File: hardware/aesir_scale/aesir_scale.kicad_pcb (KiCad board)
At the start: 2 copper layers, 60 x 50 mm, 48 parts, among them J1 jst xh 4, J2 jst gh, J3 jst xh 4, J4 jst_sh 6, J5 jst gh, J6 USB_C_Receptacle_USB2.0, U1 STM32U575CGTx, U2 NAU7802SGI, U3 AZ1117CH2-3.3TRG1, U4 TJA1051T, Y1 48MHz

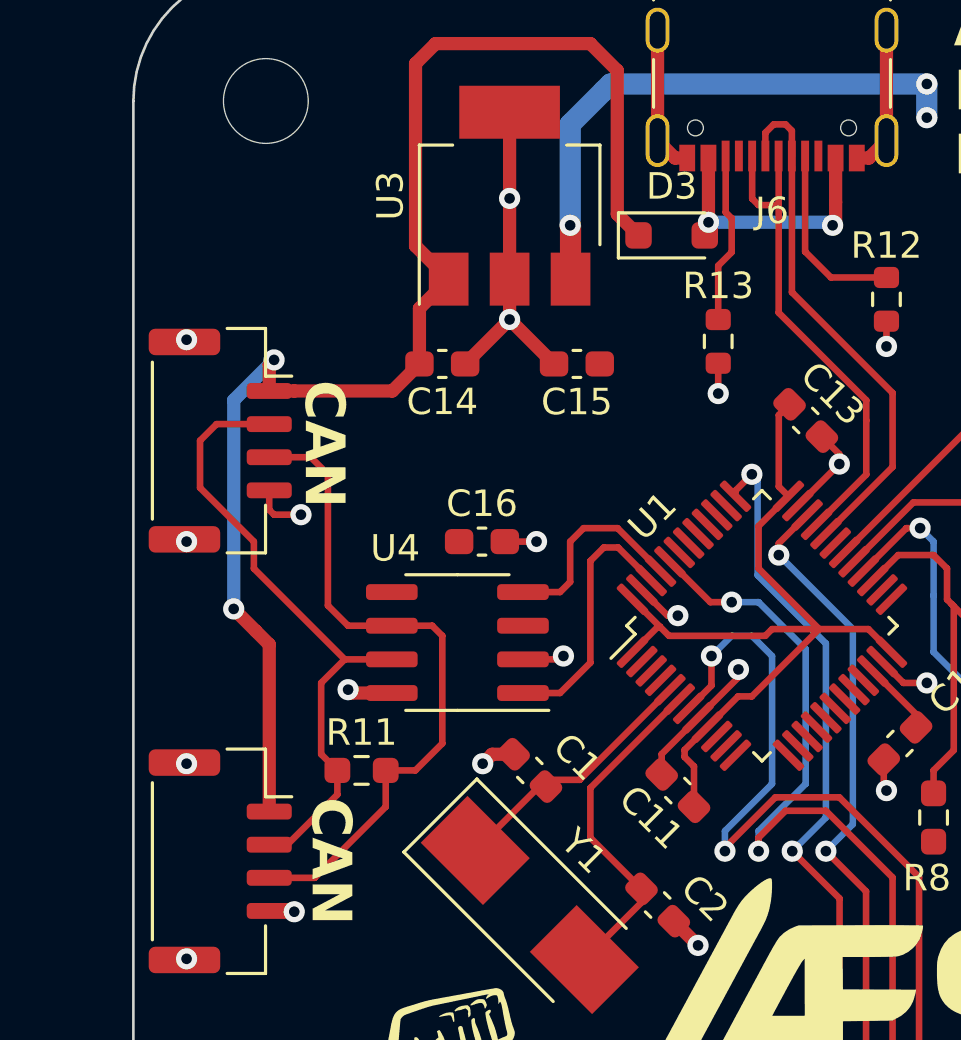
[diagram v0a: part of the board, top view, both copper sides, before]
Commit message: USB diode & CAN jumper
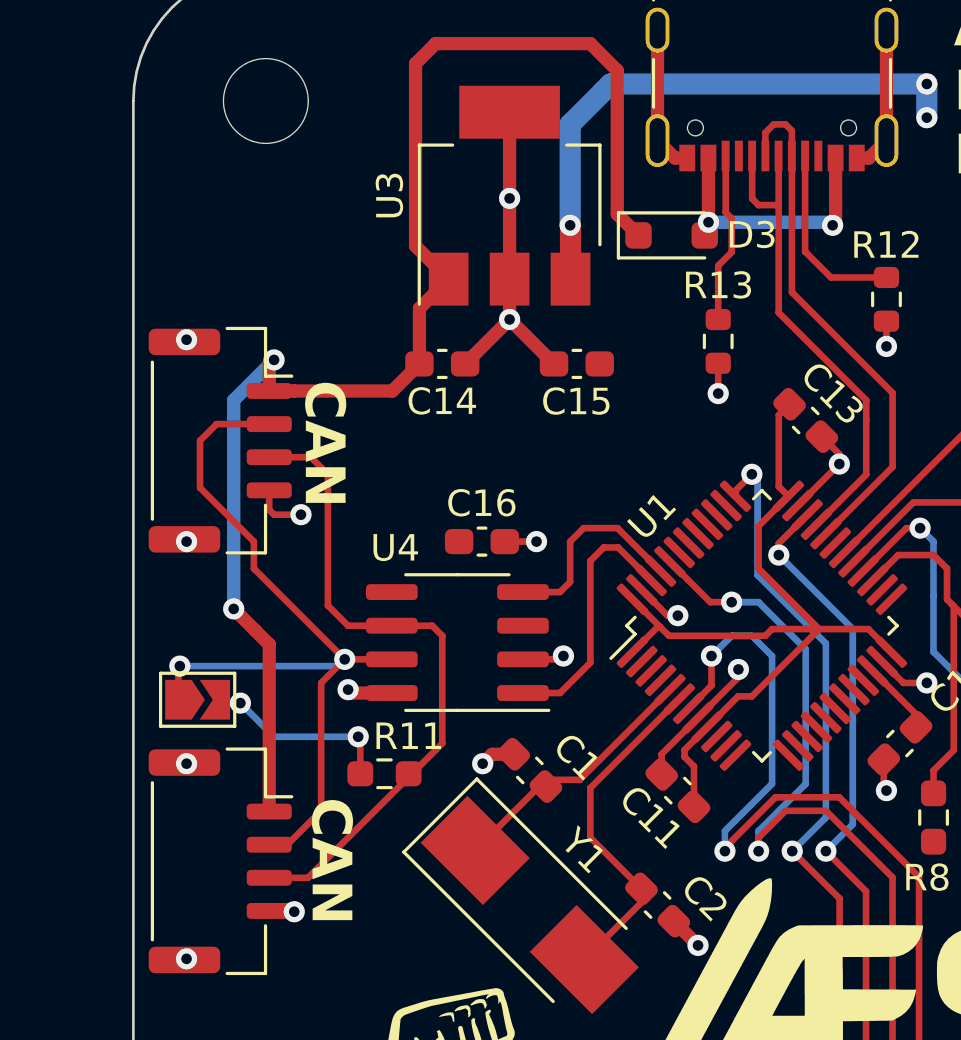
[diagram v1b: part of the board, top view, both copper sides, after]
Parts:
- added JP1: SolderJumper_2_Open, Jumper:SolderJumper-2_P1.3mm_Open_TrianglePad1.0x1.5mm, F.Cu at (64.4, 93.6)
- moved R11 0.87 mm to (71.5, 96.4)
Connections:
- R11 pad 1: /CAN_H -> Net-(JP1-B)
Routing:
- net Net-(JP1-B): track 0.00 -> 7.34 mm, vias 0 -> 2
- net /CAN_H: track 24.2 -> 31.4 mm, vias 0 -> 2
- net /CAN_L: track 26.2 -> 24.9 mm
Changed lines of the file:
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@@
   (net 62 "VCC")
   (net 63 "Net-(D3-A)")
+  (net 64 "Net-(JP1-B)")
   (footprint "Package_SO:SOIC-8_3.9x4.9mm_P1.27mm" (layer "F.Cu")
     (at 74.23 91.44 180)
@@
     (property "mfn" " USB4105-GF-A ")
     (attr smd)
-    (fp_text reference "J6" (at 0 -4.58) (layer "F.SilkS")
+    (fp_text reference "J6" (at 0 -4.58) (layer "F.SilkS") hide
         (effects (font (size 1 1) (thickness 0.15)))
     )
@@
   )
   (footprint "Resistor_SMD:R_0603_1608Metric_Pad0.98x0.95mm_HandSolder" (layer "F.Cu")
-    (at 70.612 96.266)
+    (at 71.4775 96.393)
     (descr "Resistor SMD 0603 (1608 Metric), square (rectangular) end terminal, IPC_7351 nominal with elongated pad for handsoldering. (Body size source: IPC-SM-782 page 72, https://www.pcb-3d.com/wordpress/wp-content/uploads/ipc-sm-782a_amendment_1_and_2.pdf), generated with kicad-footprint-generator")
     (tags "resistor handsolder")
@@
     (property "ki_keywords" "R resistor")
     (attr smd)
-    (fp_text reference "R11" (at 0 -1.43) (layer "F.SilkS")
+    (fp_text reference "R11" (at 0.9125 -1.397) (layer "F.SilkS")
         (effects (font (size 1 1) (thickness 0.15)))
     )
@@
       (stroke (width 0.1) (type solid)) (layer "F.Fab"))
     (pad "1" smd roundrect (at -0.9125 0) (size 0.975 0.95) (layers "F.Cu" "F.Paste" "F.Mask") (roundrect_rratio 0.25)
-      (net 32 "/CAN_H") (pintype "passive"))
+      (net 64 "Net-(JP1-B)") (pintype "passive"))
     (pad "2" smd roundrect (at 0.9125 0) (size 0.975 0.95) (layers "F.Cu" "F.Paste" "F.Mask") (roundrect_rratio 0.25)
       (net 33 "/CAN_L") (pintype "passive"))
@@
     (property "ki_keywords" "diode")
     (attr smd)
-    (fp_text reference "D3" (at 0 -1.85) (layer "F.SilkS")
+    (fp_text reference "D3" (at 3.028 0) (layer "F.SilkS")
         (effects (font (size 1 1) (thickness 0.15)))
     )
@@
     )
   )
+  (footprint "Jumper:SolderJumper-2_P1.3mm_Open_TrianglePad1.0x1.5mm" (layer "F.Cu")
+    (at 64.426 93.599)
+    (descr "SMD Solder Jumper, 1x1.5mm Triangular Pads, 0.3mm gap, open")
+    (tags "solder jumper open")
+    (property "Sheetfile" "aesir_scale.kicad_sch")
+    (property "Sheetname" "")
+    (property "ki_description" "Solder Jumper, 2-pole, open")
+    (property "ki_keywords" "solder jumper SPST")
+    (attr exclude_from_pos_files)
+    (fp_text reference "JP1" (at 0 -1.8) (layer "F.SilkS") hide
+        (effects (font (size 1 1) (thickness 0.15)))
+    )
+    (fp_text value "SolderJumper_2_Open" (at 0 1.9) (layer "F.Fab")
+        (effects (font (size 1 1) (thickness 0.15)))
+    )
+    (fp_line (start -1.4 -1) (end 1.4 -1)
+      (stroke (width 0.12) (type solid)) (layer "F.SilkS"))
+    (fp_line (start -1.4 1) (end -1.4 -1)
+      (stroke (width 0.12) (type solid)) (layer "F.SilkS"))
+    (fp_line (start 1.4 -1) (end 1.4 1)
+      (stroke (width 0.12) (type solid)) (layer "F.SilkS"))
+    (fp_line (start 1.4 1) (end -1.4 1)
+      (stroke (width 0.12) (type solid)) (layer "F.SilkS"))
+    (fp_line (start -1.65 -1.25) (end -1.65 1.25)
+      (stroke (width 0.05) (type solid)) (layer "F.CrtYd"))
+    (fp_line (start -1.65 -1.25) (end 1.65 -1.25)
+      (stroke (width 0.05) (type solid)) (layer "F.CrtYd"))
+    (fp_line (start 1.65 1.25) (end -1.65 1.25)
+      (stroke (width 0.05) (type solid)) (layer "F.CrtYd"))
+    (fp_line (start 1.65 1.25) (end 1.65 -1.25)
+      (stroke (width 0.05) (type solid)) (layer "F.CrtYd"))
+    (pad "1" smd custom (at -0.725 0) (size 0.3 0.3) (layers "F.Cu" "F.Mask")
+      (net 32 "/CAN_H") (pinfunction "A") (pintype "passive") (zone_connect 2) (thermal_bridge_angle 45)
+      (options (clearance outline) (anchor rect))
+      (primitives
+        (gr_poly
+          (pts
+            (xy 1 0)
+            (xy 0.5 0.75)
+            (xy -0.5 0.75)
+            (xy -0.5 -0.75)
+            (xy 0.5 -0.75)
+          )
+          (width 0) (fill yes))
+      ))
+    (pad "2" smd custom (at 0.725 0) (size 0.3 0.3) (layers "F.Cu" "F.Mask")
+      (net 64 "Net-(JP1-B)") (pinfunction "B") (pintype "passive") (zone_connect 2) (thermal_bridge_angle 45)
+      (options (clearance outline) (anchor rect))
+      (primitives
+        (gr_poly
+          (pts
+            (xy 0.5 0.75)
+            (xy -0.65 0.75)
+            (xy -0.15 0)
+            (xy -0.65 -0.75)
+            (xy 0.5 -0.75)
+          )
+          (width 0) (fill yes))
+      ))
+  )
   (footprint "LED_SMD:LED_0805_2012Metric_Pad1.15x1.40mm_HandSolder" (layer "F.Cu")
     (at 108.78725 79.502 180)
@@
   (segment (start 80.01 70.358) (end 91.948 70.358) (width 0.8) (layer "B.Cu") (net 13))
   (segment (start 79.756 70.612) (end 80.01 70.358) (width 0.8) (layer "B.Cu") (net 13))
-  (segment (start 67.808 99.07) (end 66.62 99.07) (width 0.25) (layer "F.Cu") (net 32))
-  (segment (start 69.088 92.964) (end 69.977 92.075) (width 0.25) (layer "F.Cu") (net 32))
-  (segment (start 69.6995 97.1785) (end 69.6995 96.266) (width 0.25) (layer "F.Cu") (net 32))
-  (segment (start 69.088 95.6545) (end 69.088 92.964) (width 0.25) (layer "F.Cu") (net 32))
+  (segment (start 63.701 92.382) (end 63.754 92.329) (width 0.25) (layer "F.Cu") (net 32))
   (segment (start 69.977 92.075) (end 66.548 88.646) (width 0.25) (layer "F.Cu") (net 32))
   (segment (start 71.755 92.075) (end 69.977 92.075) (width 0.25) (layer "F.Cu") (net 32))
+  (segment (start 69.977 92.075) (end 69.088 92.964) (width 0.25) (layer "F.Cu") (net 32))
   (segment (start 64.516 83.82) (end 64.516 85.598) (width 0.25) (layer "F.Cu") (net 32))
   (segment (start 66.62 83.195) (end 65.141 83.195) (width 0.25) (layer "F.Cu") (net 32))
-  (segment (start 69.6995 96.266) (end 69.088 95.6545) (width 0.25) (layer "F.Cu") (net 32))
+  (segment (start 63.701 93.599) (end 63.701 92.382) (width 0.25) (layer "F.Cu") (net 32))
+  (segment (start 67.808 99.07) (end 66.62 99.07) (width 0.25) (layer "F.Cu") (net 32))
+  (segment (start 69.088 97.79) (end 67.808 99.07) (width 0.25) (layer "F.Cu") (net 32))
+  (segment (start 69.088 92.964) (end 69.088 97.79) (width 0.25) (layer "F.Cu") (net 32))
   (segment (start 66.548 88.646) (end 66.548 87.63) (width 0.25) (layer "F.Cu") (net 32))
   (segment (start 65.141 83.195) (end 64.516 83.82) (width 0.25) (layer "F.Cu") (net 32))
   (segment (start 64.516 85.598) (end 66.548 87.63) (width 0.25) (layer "F.Cu") (net 32))
-  (segment (start 69.041 97.837) (end 67.808 99.07) (width 0.25) (layer "F.Cu") (net 32))
-  (segment (start 69.041 97.837) (end 69.6995 97.1785) (width 0.25) (layer "F.Cu") (net 32))
+  (via (at 63.754 92.329) (size 0.8) (drill 0.4) (layers "F.Cu" "B.Cu") (net 32))
+  (via (at 69.977 92.075) (size 0.8) (drill 0.4) (layers "F.Cu" "B.Cu") (net 32))
+  (segment (start 69.723 92.329) (end 69.977 92.075) (width 0.25) (layer "B.Cu") (net 32))
+  (segment (start 63.754 92.329) (end 69.723 92.329) (width 0.25) (layer "B.Cu") (net 32))
   (segment (start 73.279 90.805) (end 73.66 91.186) (width 0.25) (layer "F.Cu") (net 33))
-  (segment (start 71.5245 97.6395) (end 68.844 100.32) (width 0.25) (layer "F.Cu") (net 33))
   (segment (start 71.755 90.805) (end 73.279 90.805) (width 0.25) (layer "F.Cu") (net 33))
   (segment (start 69.342 85.09) (end 69.342 90.043) (width 0.25) (layer "F.Cu") (net 33))
+  (segment (start 73.66 95.25) (end 68.59 100.32) (width 0.25) (layer "F.Cu") (net 33))
   (segment (start 70.104 90.805) (end 71.755 90.805) (width 0.25) (layer "F.Cu") (net 33))
   (segment (start 68.697 84.445) (end 69.342 85.09) (width 0.25) (layer "F.Cu") (net 33))
   (segment (start 67.128 84.445) (end 68.697 84.445) (width 0.25) (layer "F.Cu") (net 33))
   (segment (start 69.342 90.043) (end 70.104 90.805) (width 0.25) (layer "F.Cu") (net 33))
-  (segment (start 71.5245 96.266) (end 72.644 96.266) (width 0.25) (layer "F.Cu") (net 33))
-  (segment (start 73.66 95.25) (end 72.644 96.266) (width 0.25) (layer "F.Cu") (net 33))
-  (segment (start 68.844 100.32) (end 66.62 100.32) (width 0.25) (layer "F.Cu") (net 33))
-  (segment (start 71.5245 96.266) (end 71.5245 97.6395) (width 0.25) (layer "F.Cu") (net 33))
   (segment (start 73.66 91.186) (end 73.66 95.25) (width 0.25) (layer "F.Cu") (net 33))
+  (segment (start 68.59 100.32) (end 67.128 100.32) (width 0.25) (layer "F.Cu") (net 33))
   (segment (start 111.125 102.87) (end 118.11 102.87) (width 0.25) (layer "F.Cu") (net 34))
   (segment (start 118.11 100.37) (end 111.165 100.37) (width 0.25) (layer "F.Cu") (net 35))
@@
   (segment (start 88.278 75.578) (end 88.392 75.692) (width 0.5) (layer "B.Cu") (net 63))
   (segment (start 83.706 75.578) (end 88.278 75.578) (width 0.5) (layer "B.Cu") (net 63))
+  (segment (start 65.278 93.726) (end 65.151 93.599) (width 0.25) (layer "F.Cu") (net 64))
+  (segment (start 70.565 96.393) (end 70.565 95.076) (width 0.25) (layer "F.Cu") (net 64))
+  (segment (start 70.565 95.076) (end 70.485 94.996) (width 0.25) (layer "F.Cu") (net 64))
+  (segment (start 66.04 93.726) (end 65.278 93.726) (width 0.25) (layer "F.Cu") (net 64))
+  (via (at 66.04 93.726) (size 0.8) (drill 0.4) (layers "F.Cu" "B.Cu") (net 64))
+  (via (at 70.485 94.996) (size 0.8) (drill 0.4) (layers "F.Cu" "B.Cu") (net 64))
+  (segment (start 70.485 94.996) (end 67.31 94.996) (width 0.25) (layer "B.Cu") (net 64))
+  (segment (start 67.31 94.996) (end 66.04 93.726) (width 0.25) (layer "B.Cu") (net 64))
   (zone (net 13) (net_name "+3V3") (layer "F.Cu") (hatch edge 0.5)
     (connect_pads (clearance 0.5))

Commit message: add caps
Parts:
- added C8: 4u7, Capacitor_SMD:C_0603_1608Metric_Pad1.08x0.95mm_HandSolder, F.Cu at (92.9, 90.2)
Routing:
- net Earth: track 63.6 -> 67.9 mm
- net +3V3: track 60.9 -> 63.0 mm
- net /SCL: track 17.0 -> 17.6 mm
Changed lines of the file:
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@@
     )
   )
+  (footprint "Capacitor_SMD:C_0603_1608Metric_Pad1.08x0.95mm_HandSolder" (layer "F.Cu")
+    (at 92.93888 90.19512 45)
+    (descr "Capacitor SMD 0603 (1608 Metric), square (rectangular) end terminal, IPC_7351 nominal with elongated pad for handsoldering. (Body size source: IPC-SM-782 page 76, https://www.pcb-3d.com/wordpress/wp-content/uploads/ipc-sm-782a_amendment_1_and_2.pdf), generated with kicad-footprint-generator")
+    (tags "capacitor handsolder")
+    (property "Sheetfile" "aesir_scale.kicad_sch")
+    (property "Sheetname" "")
+    (property "ki_description" "Unpolarized capacitor, small symbol")
+    (property "ki_keywords" "capacitor cap")
+    (attr smd)
+    (fp_text reference "C8" (at 1.113156 -1.436841 45) (layer "F.SilkS")
+        (effects (font (size 1 1) (thickness 0.15)))
+    )
+    (fp_text value "4u7" (at 0 1.43 45) (layer "F.Fab")
+        (effects (font (size 1 1) (thickness 0.15)))
+    )
+    (fp_text user "${REFERENCE}" (at 0 0 45) (layer "F.Fab")
+        (effects (font (size 0.4 0.4) (thickness 0.06)))
+    )
+    (fp_line (start -0.146267 -0.51) (end 0.146267 -0.51)
+      (stroke (width 0.12) (type solid)) (layer "F.SilkS"))
+    (fp_line (start -0.146267 0.51) (end 0.146267 0.51)
+      (stroke (width 0.12) (type solid)) (layer "F.SilkS"))
+    (fp_line (start -1.65 -0.73) (end 1.65 -0.73)
+      (stroke (width 0.05) (type solid)) (layer "F.CrtYd"))
+    (fp_line (start -1.65 0.73) (end -1.65 -0.73)
+      (stroke (width 0.05) (type solid)) (layer "F.CrtYd"))
+    (fp_line (start 1.65 -0.73) (end 1.65 0.73)
+      (stroke (width 0.05) (type solid)) (layer "F.CrtYd"))
+    (fp_line (start 1.65 0.73) (end -1.65 0.73)
+      (stroke (width 0.05) (type solid)) (layer "F.CrtYd"))
+    (fp_line (start -0.8 -0.4) (end 0.8 -0.4)
+      (stroke (width 0.1) (type solid)) (layer "F.Fab"))
+    (fp_line (start -0.8 0.4) (end -0.8 -0.4)
+      (stroke (width 0.1) (type solid)) (layer "F.Fab"))
+    (fp_line (start 0.8 -0.4) (end 0.8 0.4)
+      (stroke (width 0.1) (type solid)) (layer "F.Fab"))
+    (fp_line (start 0.8 0.4) (end -0.8 0.4)
+      (stroke (width 0.1) (type solid)) (layer "F.Fab"))
+    (pad "1" smd roundrect (at -0.8625 0 45) (size 1.075 0.95) (layers "F.Cu" "F.Paste" "F.Mask") (roundrect_rratio 0.25)
+      (net 13 "+3V3") (pintype "passive"))
+    (pad "2" smd roundrect (at 0.8625 0 45) (size 1.075 0.95) (layers "F.Cu" "F.Paste" "F.Mask") (roundrect_rratio 0.25)
+      (net 12 "Earth") (pintype "passive"))
+    (model "${KICAD6_3DMODEL_DIR}/Capacitor_SMD.3dshapes/C_0603_1608Metric.wrl"
+      (offset (xyz 0 0 0))
+      (scale (xyz 1 1 1))
+      (rotate (xyz 0 0 0))
+    )
+  )
   (footprint "Resistor_SMD:R_0603_1608Metric_Pad0.98x0.95mm_HandSolder" (layer "F.Cu")
     (at 98.552 112.3715 90)
@@
   (segment (start 76.35212 95.65612) (end 75.53988 95.65612) (width 0.5) (layer "F.Cu") (net 12))
   (segment (start 92.954 114.818) (end 92.964 114.808) (width 0.5) (layer "F.Cu") (net 12))
+  (segment (start 91.948 92.964) (end 93.853 91.059) (width 0.25) (layer "F.Cu") (net 12))
   (segment (start 67.128 85.695) (end 67.128 86.432) (width 0.25) (layer "F.Cu") (net 12))
   (segment (start 83.311998 94.278662) (end 81.94012 95.65054) (width 0.25) (layer "F.Cu") (net 12))
@@
   (segment (start 98.3985 97.536) (end 100.4835 97.536) (width 0.5) (layer "F.Cu") (net 12))
   (segment (start 74.5225 80.924) (end 76.2 79.2465) (width 0.5) (layer "F.Cu") (net 12))
+  (segment (start 93.853 91.059) (end 93.853 89.88948) (width 0.25) (layer "F.Cu") (net 12))
   (segment (start 81.94012 95.65054) (end 81.94012 96.41812) (width 0.25) (layer "F.Cu") (net 12))
   (segment (start 96.7867 86.7675) (end 97.8905 86.7675) (width 0.5) (layer "F.Cu") (net 12))
   (segment (start 75.53988 95.65612) (end 75.184 96.012) (width 0.5) (layer "F.Cu") (net 12))
+  (segment (start 93.853 89.88948) (end 93.54876 89.58524) (width 0.25) (layer "F.Cu") (net 12))
   (segment (start 109.81225 79.502) (end 111.07325 79.502) (width 0.25) (layer "F.Cu") (net 12))
   (segment (start 67.128 86.432) (end 67.31 86.614) (width 0.25) (layer "F.Cu") (net 12))
@@
   (segment (start 83.665551 94.632215) (end 84.825766 93.472) (width 0.25) (layer "F.Cu") (net 13))
   (segment (start 85.344 93.472) (end 84.825766 93.472) (width 0.25) (layer "F.Cu") (net 13))
+  (segment (start 92.329 90.805) (end 91.611664 90.805) (width 0.25) (layer "F.Cu") (net 13))
   (segment (start 82.804 95.493766) (end 82.804 95.758) (width 0.25) (layer "F.Cu") (net 13))
   (segment (start 85.598 87.042912) (end 85.598 88.646) (width 0.25) (layer "F.Cu") (net 13))
   (segment (start 86.723788 85.917124) (end 85.598 87.042912) (width 0.25) (layer "F.Cu") (net 13))
   (segment (start 86.36 85.553336) (end 86.36 82.85424) (width 0.25) (layer "F.Cu") (net 13))
+  (segment (start 91.611664 90.805) (end 90.612876 91.803788) (width 0.25) (layer "F.Cu") (net 13))
   (segment (start 86.654 109.26) (end 86.614 109.22) (width 0.5) (layer "F.Cu") (net 13))
   (segment (start 85.598 88.646) (end 87.884 90.932) (width 0.25) (layer "F.Cu") (net 13))
@@
   (segment (start 95.25 87.884) (end 95.25 90.17) (width 0.25) (layer "F.Cu") (net 40))
   (segment (start 93.51666 86.15066) (end 95.25 87.884) (width 0.25) (layer "F.Cu") (net 40))
-  (segment (start 92.88875 89.99125) (end 93.98 91.0825) (width 0.25) (layer "F.Cu") (net 41))
+  (segment (start 92.202 88.138) (end 94.107 88.138) (width 0.25) (layer "F.Cu") (net 41))
+  (segment (start 92.837 92.837) (end 93.8265 91.8475) (width 0.25) (layer "F.Cu") (net 41))
+  (segment (start 92.202 97.1315) (end 92.202 95.631) (width 0.25) (layer "F.Cu") (net 41))
+  (segment (start 94.742 88.773) (end 94.488 88.519) (width 0.25) (layer "F.Cu") (net 41))
+  (segment (start 92.837 94.996) (end 92.837 92.837) (width 0.25) (layer "F.Cu") (net 41))
   (segment (start 89.905769 89.099105) (end 90.866874 88.138) (width 0.25) (layer "F.Cu") (net 41))
-  (segment (start 92.71 89.8125) (end 92.88875 89.99125) (width 0.25) (layer "F.Cu") (net 41))
-  (segment (start 92.71 88.646) (end 92.71 89.8125) (width 0.25) (layer "F.Cu") (net 41))
-  (segment (start 92.964 90.0665) (end 92.88875 89.99125) (width 0.25) (layer "F.Cu") (net 41))
-  (segment (start 92.202 97.1315) (end 92.202 96.266) (width 0.25) (layer "F.Cu") (net 41))
-  (segment (start 92.964 95.504) (end 92.964 90.0665) (width 0.25) (layer "F.Cu") (net 41))
-  (segment (start 92.202 96.266) (end 92.964 95.504) (width 0.25) (layer "F.Cu") (net 41))
-  (segment (start 96.7867 91.8475) (end 94.745 91.8475) (width 0.25) (layer "F.Cu") (net 41))
+  (segment (start 95.123 91.8475) (end 94.742 91.4665) (width 0.25) (layer "F.Cu") (net 41))
+  (segment (start 94.742 91.4665) (end 94.742 88.773) (width 0.25) (layer "F.Cu") (net 41))
+  (segment (start 96.7867 91.8475) (end 95.123 91.8475) (width 0.25) (layer "F.Cu") (net 41))
   (segment (start 90.866874 88.138) (end 92.202 88.138) (width 0.25) (layer "F.Cu") (net 41))
-  (segment (start 94.745 91.8475) (end 93.98 91.0825) (width 0.25) (layer "F.Cu") (net 41))
-  (segment (start 92.202 88.138) (end 92.71 88.646) (width 0.25) (layer "F.Cu") (net 41))
+  (segment (start 93.8265 91.8475) (end 95.123 91.8475) (width 0.25) (layer "F.Cu") (net 41))
+  (segment (start 92.202 95.631) (end 92.837 94.996) (width 0.25) (layer "F.Cu") (net 41))
+  (segment (start 94.107 88.138) (end 94.488 88.519) (width 0.25) (layer "F.Cu") (net 41))
   (segment (start 89.552215 88.745551) (end 91.175766 87.122) (width 0.25) (layer "F.Cu") (net 44))
   (segment (start 93.98 93.5755) (end 93.98 97.1315) (width 0.25) (layer "F.Cu") (net 44))
